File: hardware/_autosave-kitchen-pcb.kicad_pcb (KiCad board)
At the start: 4 copper layers, 82.6 x 82.5 mm, 97 parts, among them J1 MEM2075-00-140-01-A, J2 Conn_01x06, J3 Conn_02x02_Odd_Even, J4 S3B-XH-SM4-TB_LF__SN_, J5 USB4105-GF-A, J6 DCJ200-10-A-K1-K, J7 Conn_02x05_Odd_Even, J8 Conn_02x03_Odd_Even, J9 Conn_02x05_Odd_Even, Q1 TEMT6000X01, SW1 SW_Push, SW2 SW_Push, SW3 RA1113112R, SW4 SW_Push, U1 MX25L3233FM2I-08G, U2 SHT30-DIS-B, U3 USBLC6-2SC6, U4 NCP1117ST33T3G, U5 ESP32-S3-WROOM-1-N8R8

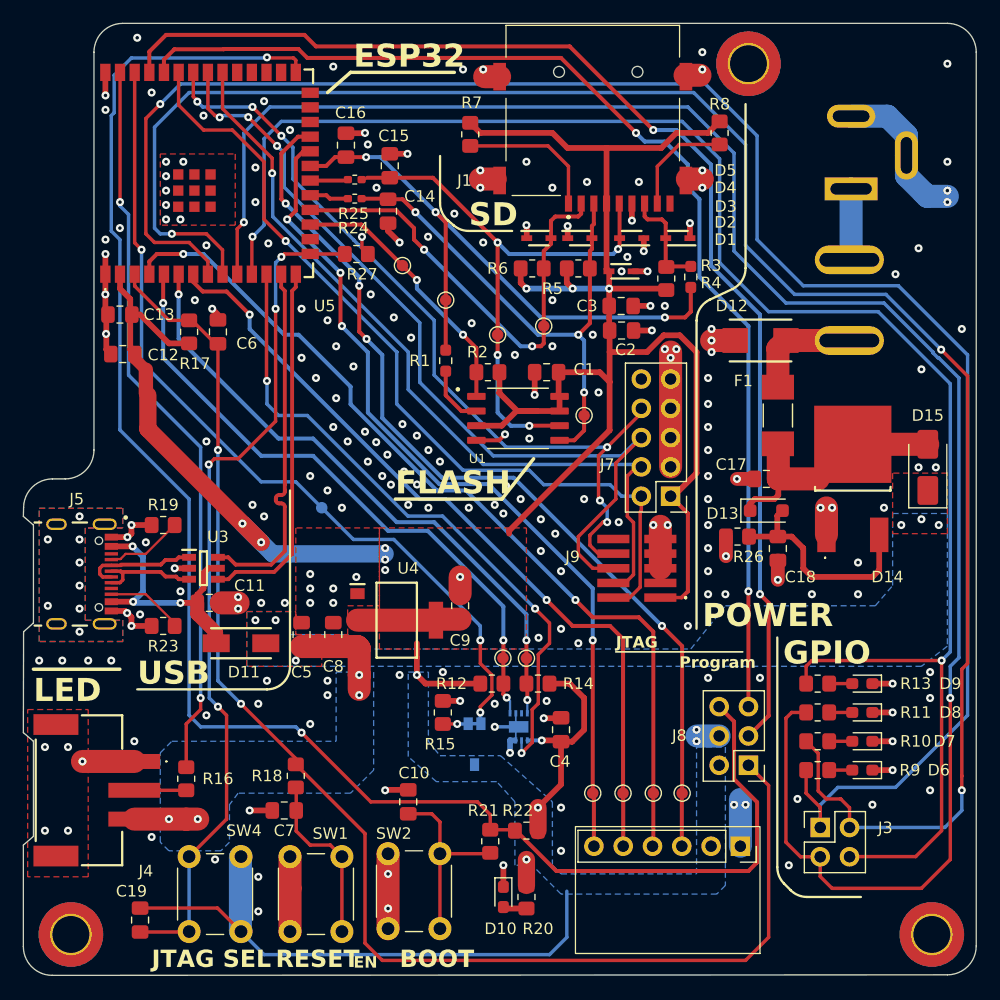
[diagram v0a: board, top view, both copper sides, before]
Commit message: Tried to prevent crosstalk, fixed silkscreen, changes to fit DFM
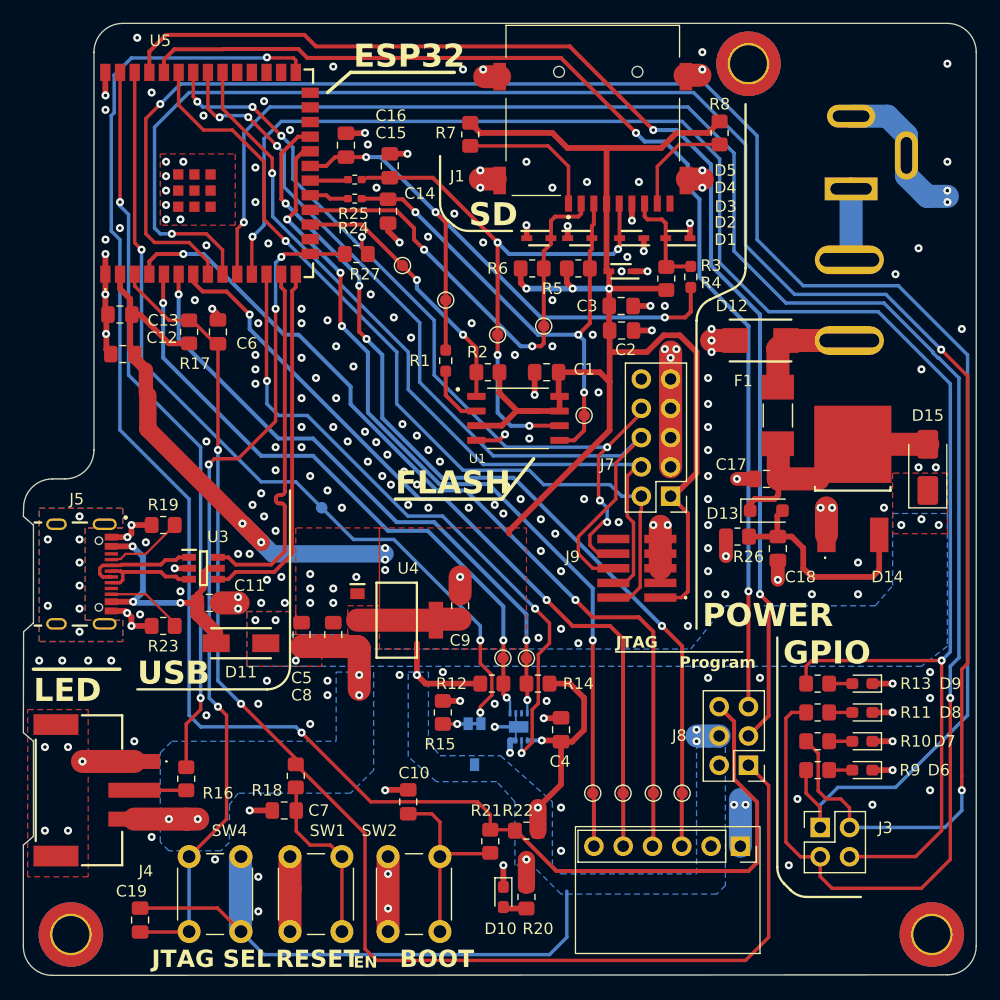
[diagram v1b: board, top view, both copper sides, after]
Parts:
- moved SW2 0.25 mm to (129.0, 137.2)
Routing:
- net GND: vias 231 -> 247
